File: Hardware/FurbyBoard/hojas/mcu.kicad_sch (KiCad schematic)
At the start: 12 parts, among them SW1 RESET, SW2 BOOT, U4 ESP32-S3-WROOM-1-N16R8

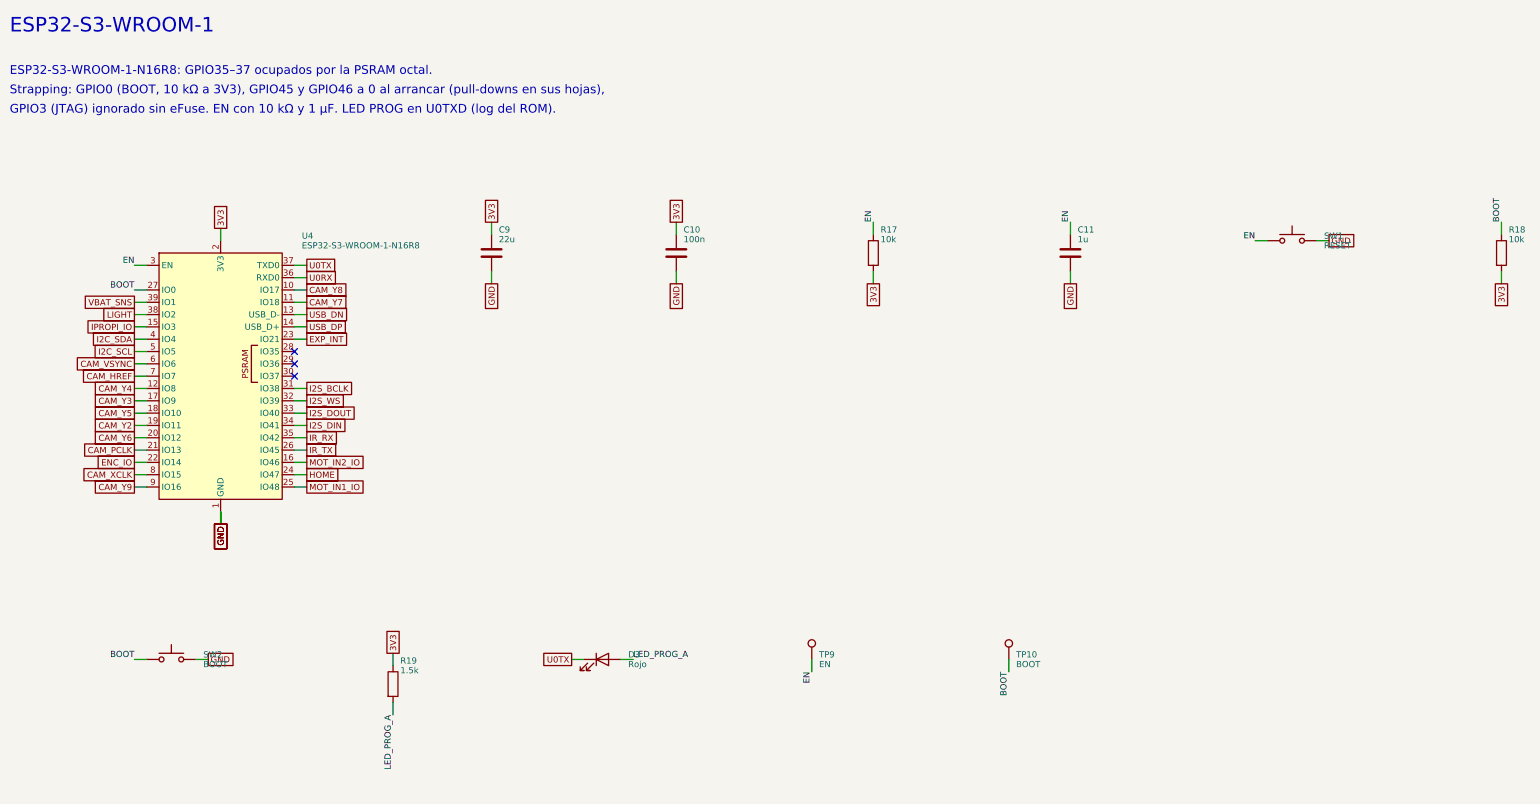
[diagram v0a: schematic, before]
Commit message: Refactor: pads de cable agrupados por zona y etiquetas globales
- Motor en J9 con leva, encoder y sensores; altavoz en J8 con inclinación y
  lengua; luz en J7 con el IR. Desaparecen J4 y J10: cada grupo sale por el
  borde más cercano a su destino.
- Micro en 2x03 en vez de 1x06 para que quepa junto al borde derecho.
- Todas las etiquetas del esquemático son globales, así el nombre de red
  coincide con el del PCB (paridad sin prefijos de hoja).
- ERC 0 errores, 0 avisos.

Co-Authored-By: Claude Opus 5.5 (1M context) <noreply@anthropic.com>
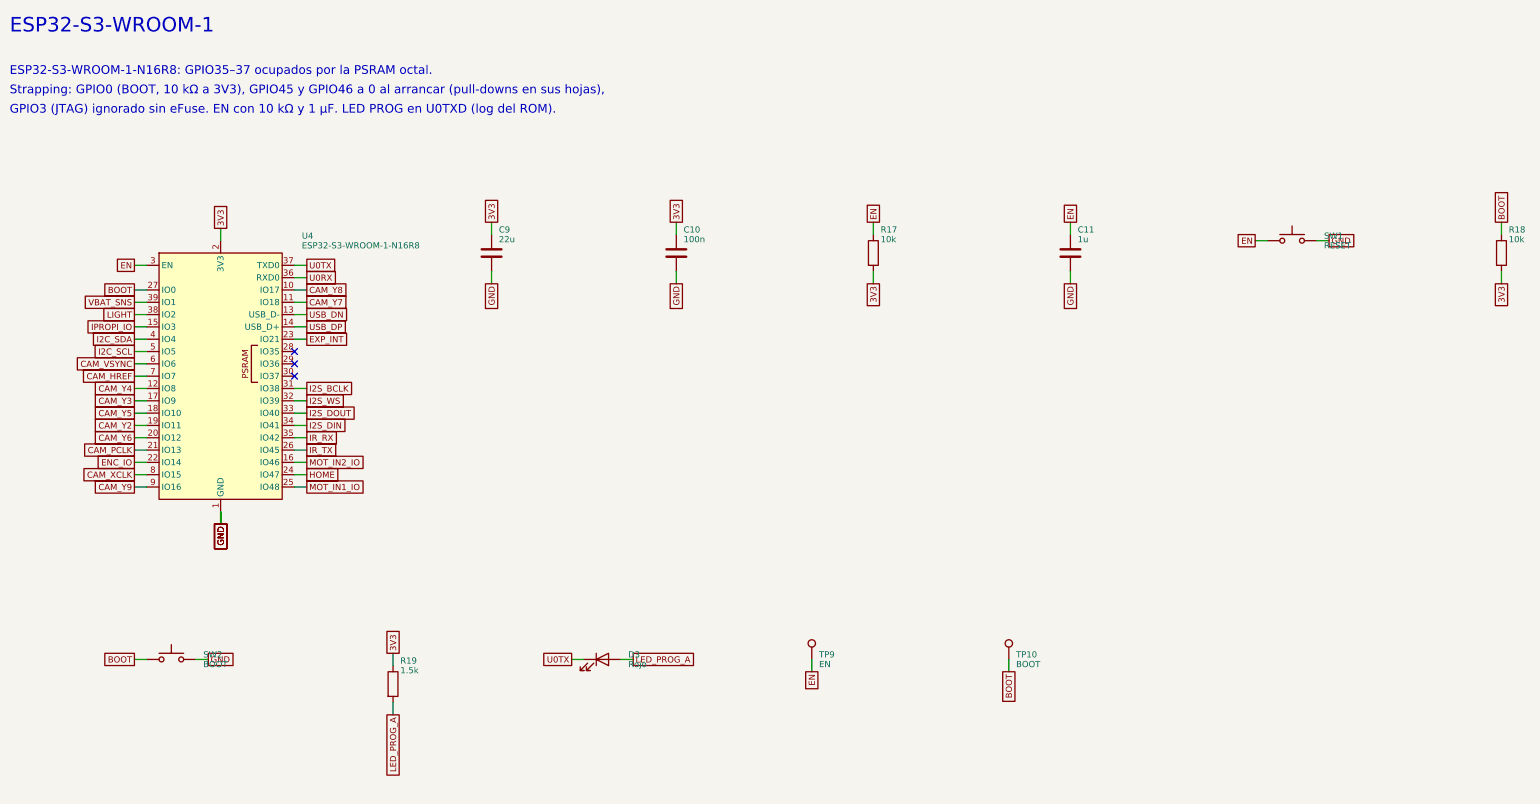
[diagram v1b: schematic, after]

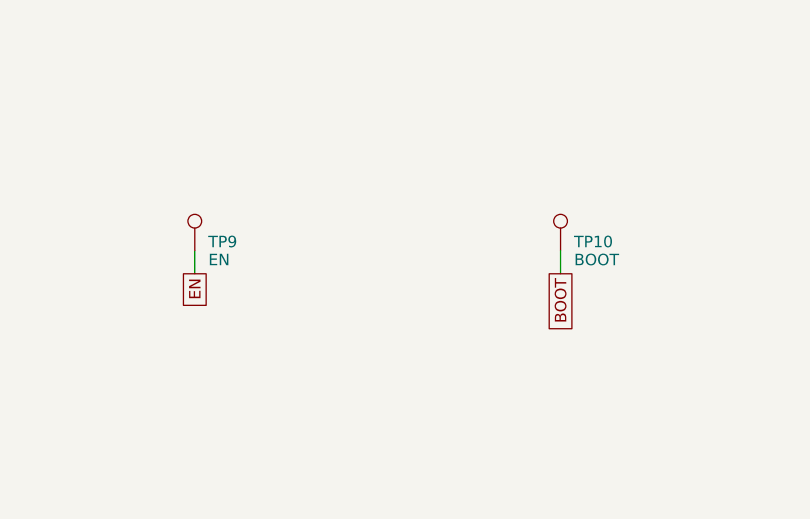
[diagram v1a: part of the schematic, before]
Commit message: Feature: par USB trazado, planos GND/VSYS y serigrafía de la FurbyBoard
- Par USB de J1 al ESD y al módulo, acoplado 0,28/0,15 por F.Cu sobre el
  plano de GND, sin vías (rutas_fijas.py, bloqueado para el autorrutado).
  Canal libre en x -83 bajo la batería.
- In1 plano de GND e In2 plano de VSYS; potencia por pista a 0,4 (cabe en
  los pads de 0,5 de paso) y 3V3 a 0,3. exportar_dsn.py deja el DSN para
  Freerouting con las clases de red.
- Rótulos de serigrafía colocados solos (serigrafia.py): TP, LED, botones,
  puentes y polaridad de la batería arriba; función de cada pad de cable y
  GPIO del J_EXP abajo, con leyenda para J7, J9 y J5.
- Para que quepan los rótulos: fila de LED con resistencias debajo, botones
  en vertical, rejilla de TP con el rótulo debajo. Quedan 14 TP: fuera EN e
  IO0 (se miden en los pads de SW1 y SW2), CHG y PG (en D1 y D2) y un GND.

ERC 0/0. DRC 0 salvo una vía de GND sin plano relleno; sin rutar.

Co-Authored-By: Claude Opus 5.5 (1M context) <noreply@anthropic.com>
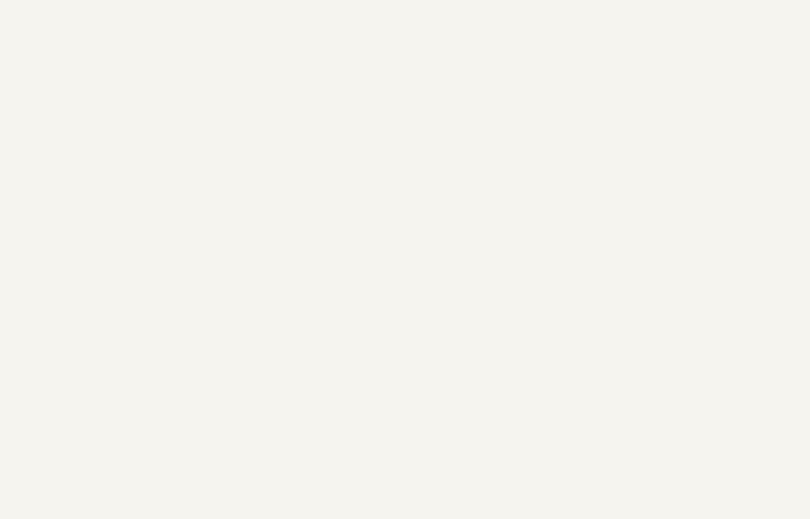
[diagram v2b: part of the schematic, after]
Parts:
- removed TP10: BOOT, TestPoint:TestPoint_Pad_D1.5mm, symbol Connector:TestPoint
- removed TP9: EN, TestPoint:TestPoint_Pad_D1.5mm, symbol Connector:TestPoint

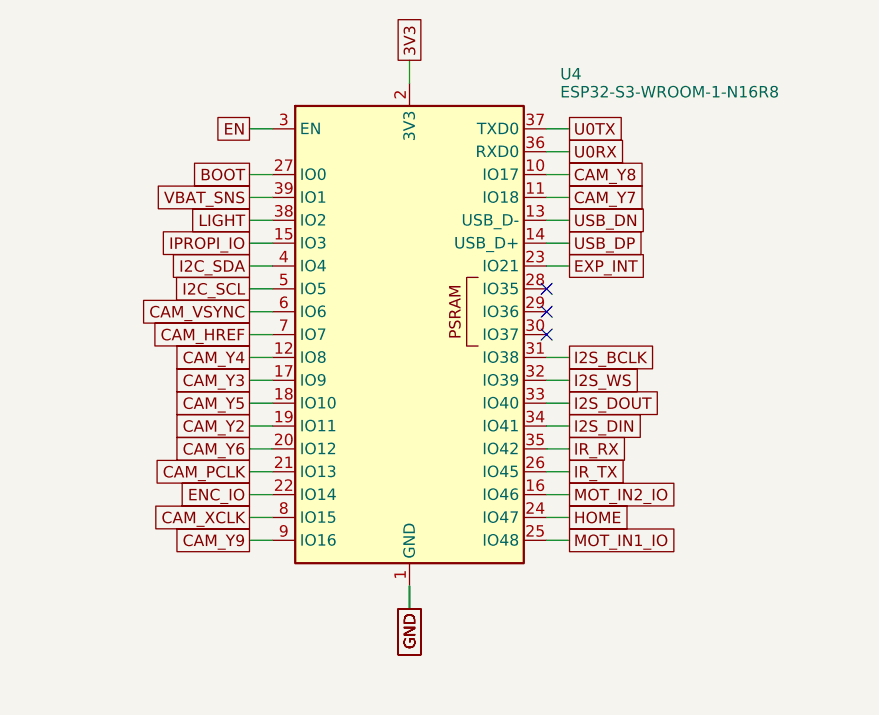
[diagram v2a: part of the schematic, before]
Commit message: Refactor: GPIO reasignados para acortar rutas e In2 como capa de señal
- Cámara en los pines del lado del FPC (fila inferior derecha y columna
  derecha del módulo), en el orden del conector para que no se crucen.
- I2S, leva, INT del expansor y encoder en la columna izquierda, hacia el
  amplificador y los sensores. MOT_IN1 pasa a GPIO9, junto a IN2 e IPROPI.
- Sin tocar strapping (IO0, IO3, IO45, IO46) ni el USB (IO19/IO20).
- In2 deja de ser plano: capa de señal con relleno de VSYS en lo libre.
  In1 sigue como GND continuo.
- Rótulos de JP1 (IO9) y JP4 (IO8) actualizados.

ERC 0/0. PCB sin rutar.

Co-Authored-By: Claude Opus 5.5 (1M context) <noreply@anthropic.com>
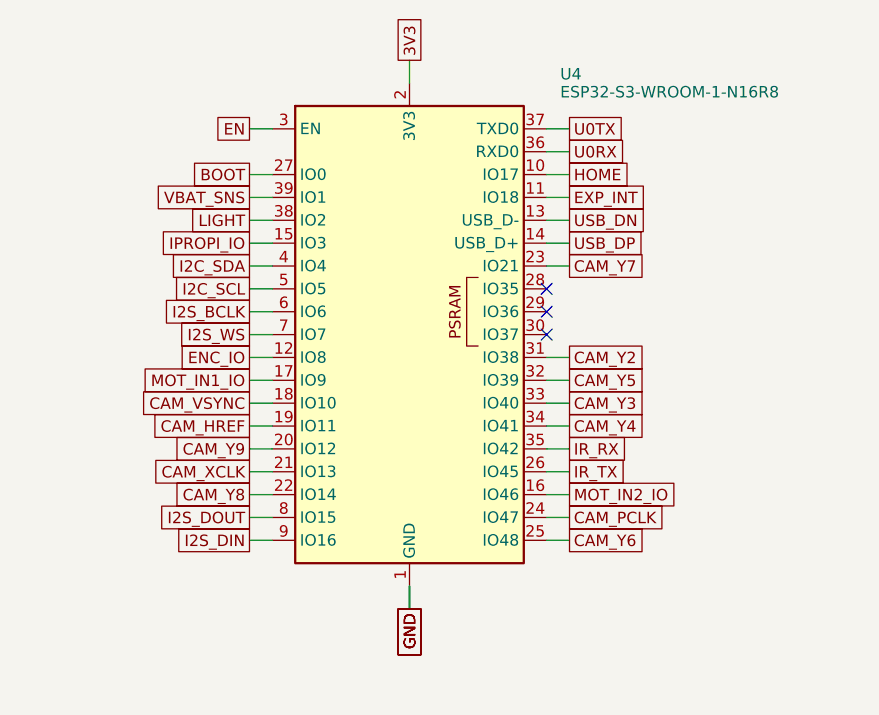
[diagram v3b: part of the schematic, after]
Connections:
- net CAM_HREF: now also U4.19 (IO11); no longer U4.7 (IO7)
- net CAM_PCLK: now also U4.24 (IO47); no longer U4.21 (IO13)
- net CAM_VSYNC: now also U4.18 (IO10); no longer U4.6 (IO6)
- net CAM_XCLK: now also U4.21 (IO13); no longer U4.8 (IO15)
- net CAM_Y2: now also U4.31 (IO38); no longer U4.19 (IO11)
- net CAM_Y3: now also U4.33 (IO40); no longer U4.17 (IO9)
- net CAM_Y4: now also U4.34 (IO41); no longer U4.12 (IO8)
- net CAM_Y5: now also U4.32 (IO39); no longer U4.18 (IO10)
- net CAM_Y6: now also U4.25 (IO48); no longer U4.20 (IO12)
- net CAM_Y7: now also U4.23 (IO21); no longer U4.11 (IO18)
- net CAM_Y8: now also U4.22 (IO14); no longer U4.10 (IO17)
- net CAM_Y9: now also U4.20 (IO12); no longer U4.9 (IO16)
- net ENC_IO: now also U4.12 (IO8); no longer U4.22 (IO14)
- net EXP_INT: now also U4.11 (IO18); no longer U4.23 (IO21)
- net HOME: now also U4.10 (IO17); no longer U4.24 (IO47)
- net I2S_BCLK: now also U4.6 (IO6); no longer U4.31 (IO38)
- net I2S_DIN: now also U4.9 (IO16); no longer U4.34 (IO41)
- net I2S_DOUT: now also U4.8 (IO15); no longer U4.33 (IO40)
- net I2S_WS: now also U4.7 (IO7); no longer U4.32 (IO39)
- net MOT_IN1_IO: now also U4.17 (IO9); no longer U4.25 (IO48)

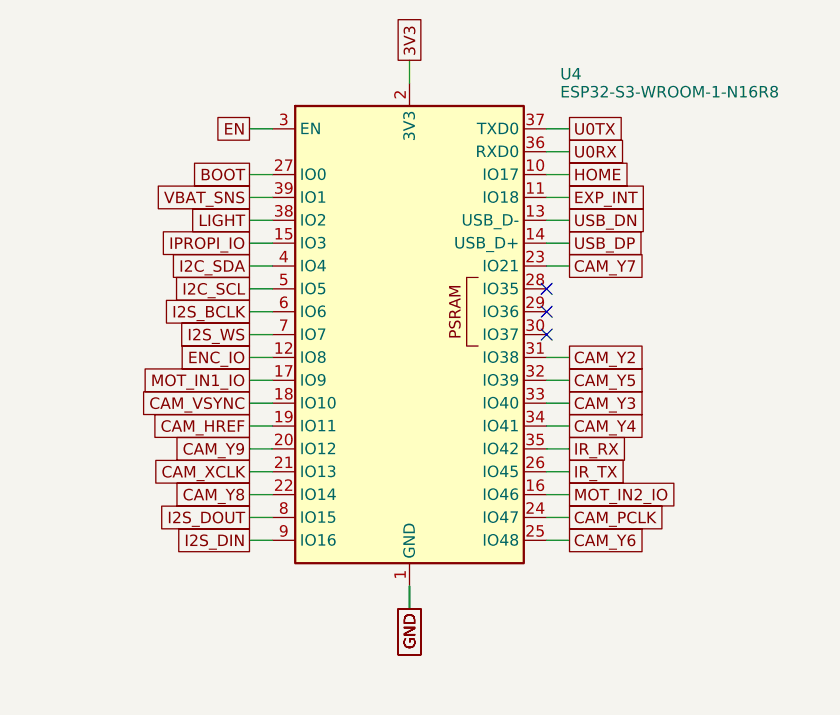
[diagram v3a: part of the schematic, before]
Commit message: Feature: esquema de la FurbyBoard al procedimiento nuevo: rúbrica L, reglas por red, pines por geometría y simulación del elevador
- Rúbrica S/M/L (L) y tabla de raíles con anchos mínimos (params.ANCHOS_MINIMOS), que gen_pro.py vuelca al .kicad_dru como una regla por red, con cuellos dentro de los patios de los QFN y de J1.
- Vías de 0,45/0,2 solo en la clase USB (cruce del par en el receptáculo de 16 pines); el resto sigue en 0,6/0,3.
- pcb-toolkit.toml: clases B/C/D, anchos, grupos explícitos y zonas del puente H y de la clase D.
- Redes a la convención: BB_SW1/2, I2S_SCK_MIC/I2S_WS_MIC.
- Pines del módulo (I2S, HOME, EXP_INT) y puertos del TCA9535 por geometría, sin tocar strapping, USB ni ADC.
- LED del encoder desde V6 por 470 ohm (sin Q2); J_EXP 2x5; J9 y J5 reordenados; serigrafía al día.
- ERC 0/0. Simulación ngspice del elevador en el peor caso (sim/). Informes de las puertas A y B en revisiones/; un crítico (NTC del cargador) queda escalado.

Co-Authored-By: Claude Fable 5.1 <noreply@anthropic.com>
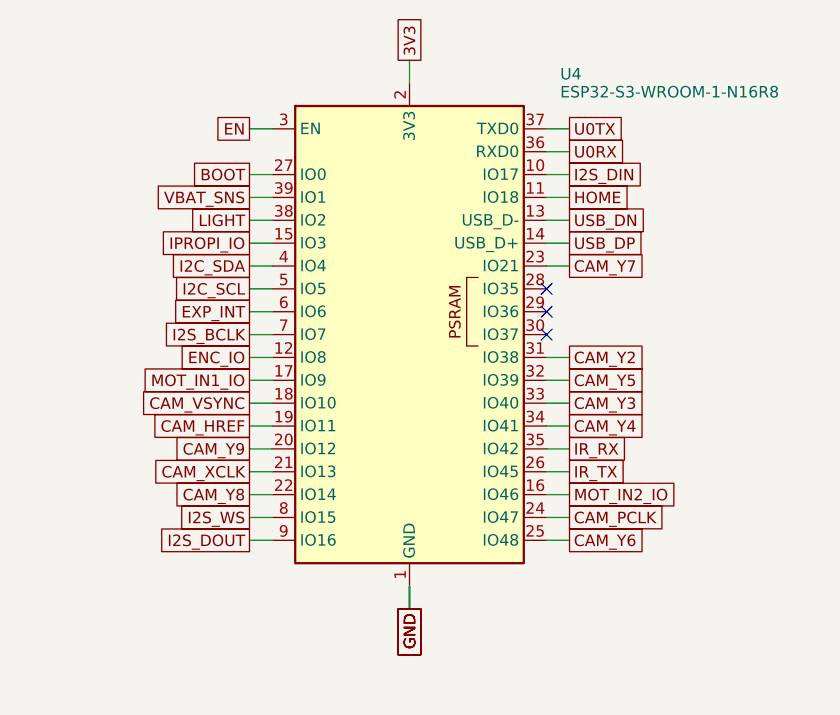
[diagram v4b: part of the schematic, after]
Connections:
- net EXP_INT: now also U4.6 (IO6); no longer U4.11 (IO18)
- net HOME: now also U4.11 (IO18); no longer U4.10 (IO17)
- net I2S_BCLK: now also U4.7 (IO7); no longer U4.6 (IO6)
- net I2S_DIN: now also U4.10 (IO17); no longer U4.9 (IO16)
- net I2S_DOUT: now also U4.9 (IO16); no longer U4.8 (IO15)
- net I2S_WS: now also U4.8 (IO15); no longer U4.7 (IO7)

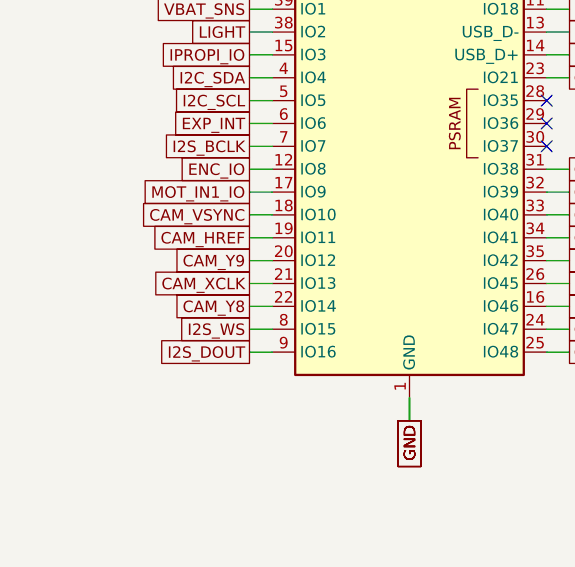
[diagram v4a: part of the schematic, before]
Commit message: Feature: series de 33 Ω en los relojes del bus DVP (M7): R59 en XCLK junto al pin 21 y R60 en PCLK junto a J6
- design.py: R59 y R60, 0402 UNI-ROYAL 33 Ω (C25105, básica); redes nuevas CAM_XCLK_IO
  (pin 21 → R59) y CAM_PCLK_CAM (J6.17 → R60). Rs + Rout ≈ Z0 (≈ 75 Ω de la pista de
  0,15 sobre In1); HREF, VSYNC y los datos no la llevan (motivo en design.py y NOTAS).
- layout.py: R59 en (−72,365; −82,35) bajo el pin 21, entre el patio del módulo y la fila
  del bus; R60 en (−53,6; −78,0) a 2 mm del pad 17 de J6.
- rutas_fijas.py: XCLK acortado por el este hasta R59.2 y entrada al pin 21 desde R59.1
  con una diagonal; PCLK baja a y −78,0 en el tramo de R60 y Y7 a −78,6 (quiebros a 45°
  escalonados). Todo en F.Cu sobre In1, sin vías nuevas.
- pcb-toolkit.toml: CAM_XCLK*/CAM_PCLK* en criticas y en el grupo DVP.

Puertas: ERC 0; DRC con paridad 0/0/0; revisar-rutado 0 errores, 152 avisos (los mismos
por tipo que antes); comprobar-flujo sin errores nuevos (los dos aceptados: I2S_DIN/clase D y
MOT_VREF/L2); rellenos: GND F 2083,0 mm² en 21 trozos (−1,6 mm² por los dos 0402), el resto
igual. PNG revisados en F.Cu a 80 px/mm: comb de J6 con R60 (PCLK y Y7 con sus quiebros,
Y6 y Y8 sin tocar) y fila sur del módulo con R59 (entrada al pin 21, Y8 y Y9 a 0,415).
Paralelos In2/In3: 28 pares, sin cambio (M1 va aparte).

Co-Authored-By: Claude Fable 5.1 <noreply@anthropic.com>
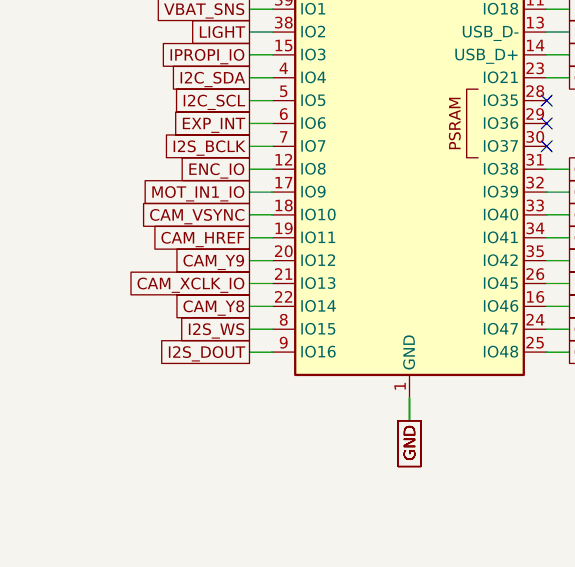
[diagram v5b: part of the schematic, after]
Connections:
- net CAM_XCLK renamed CAM_XCLK_IO
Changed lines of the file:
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@@
 		)
 	)
-	(global_label "CAM_XCLK"
+	(global_label "CAM_XCLK_IO"
 		(shape passive)
 		(at 45.72 109.22 180)
